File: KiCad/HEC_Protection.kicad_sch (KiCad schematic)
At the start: 16 parts, among them U11 74LS00, U11 74LS32, U12 74LS04, U17 74LS74, U18 74LS74, U19 74LS30, U22 74LS02, U23 74LS30, U24 74LS74, U25 74LS541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

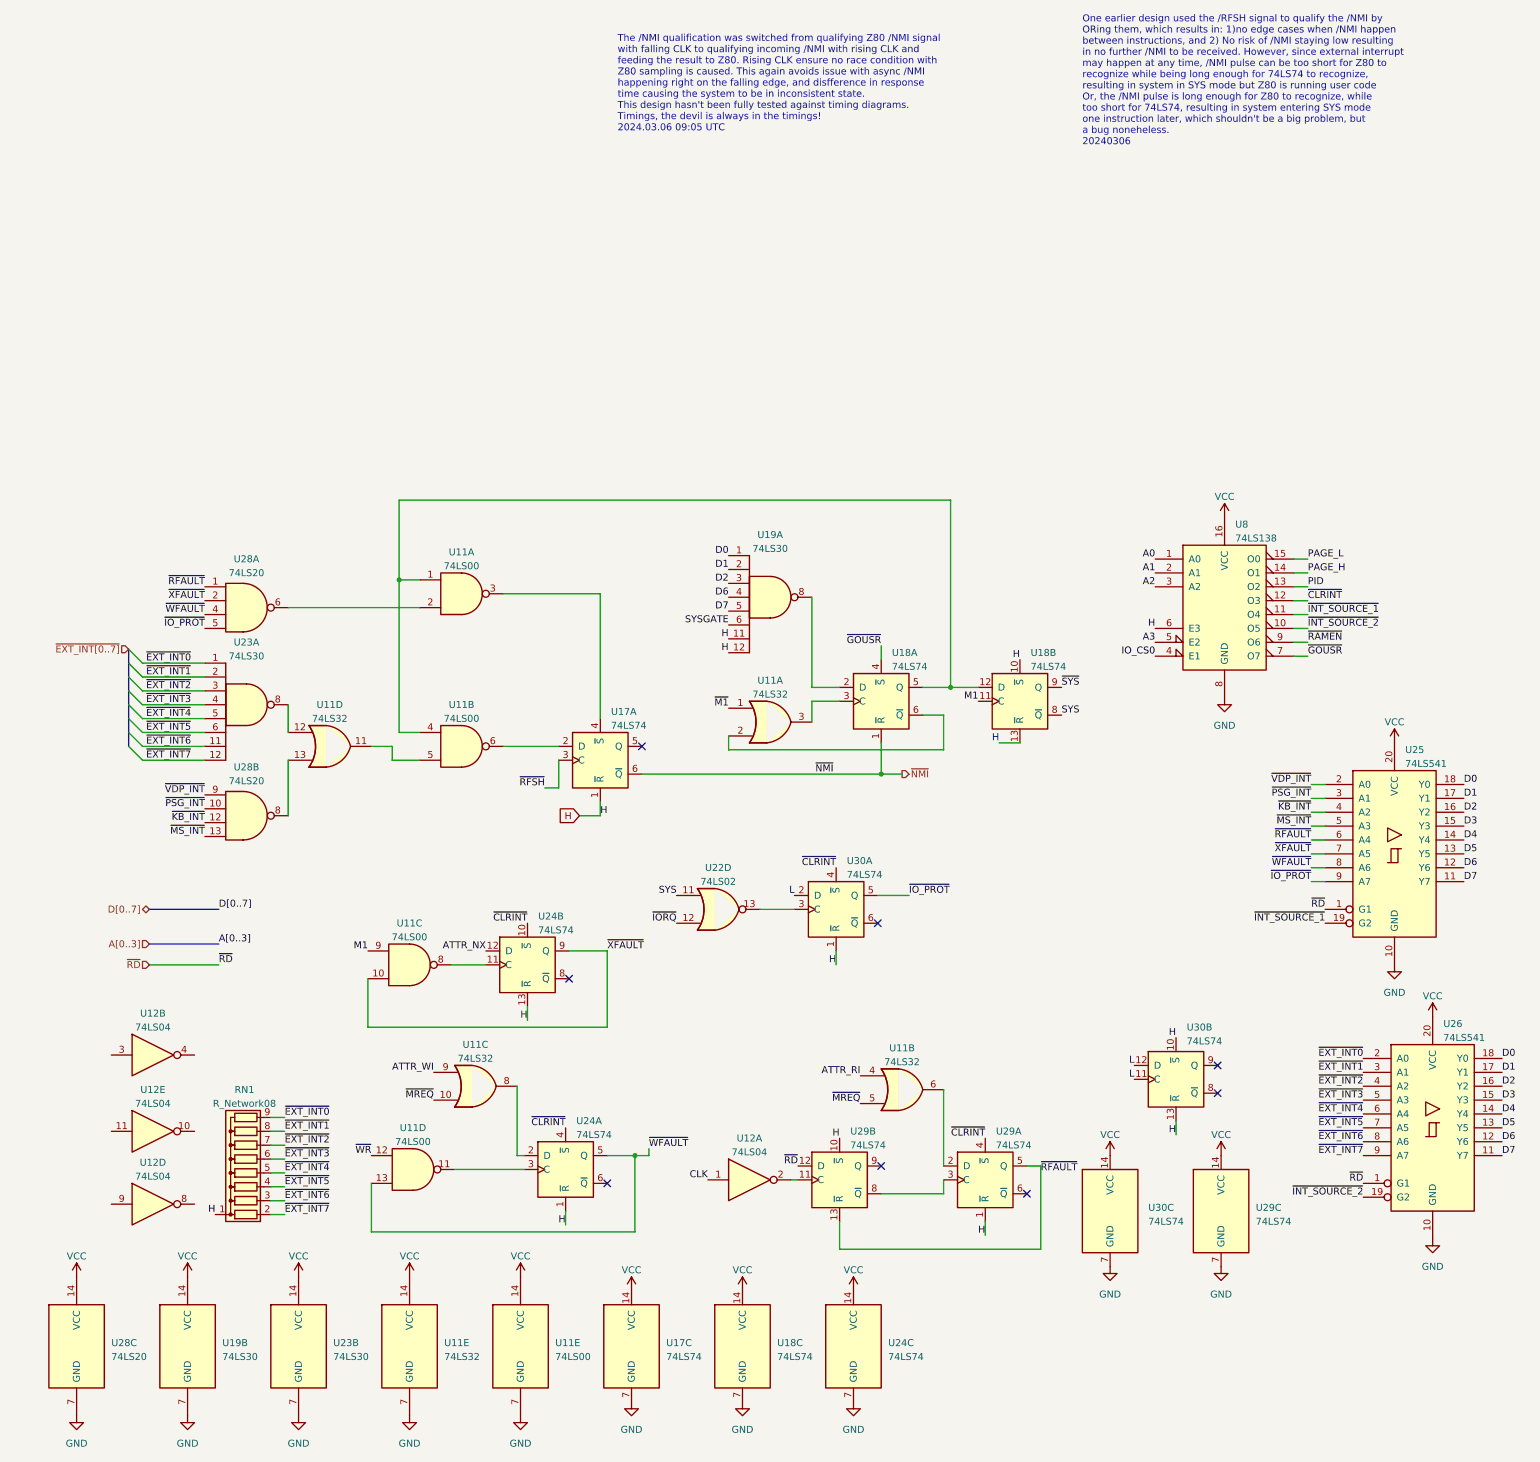
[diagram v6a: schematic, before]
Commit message: IO implementation
Implemented most of IO functions, add connections between the schematics.
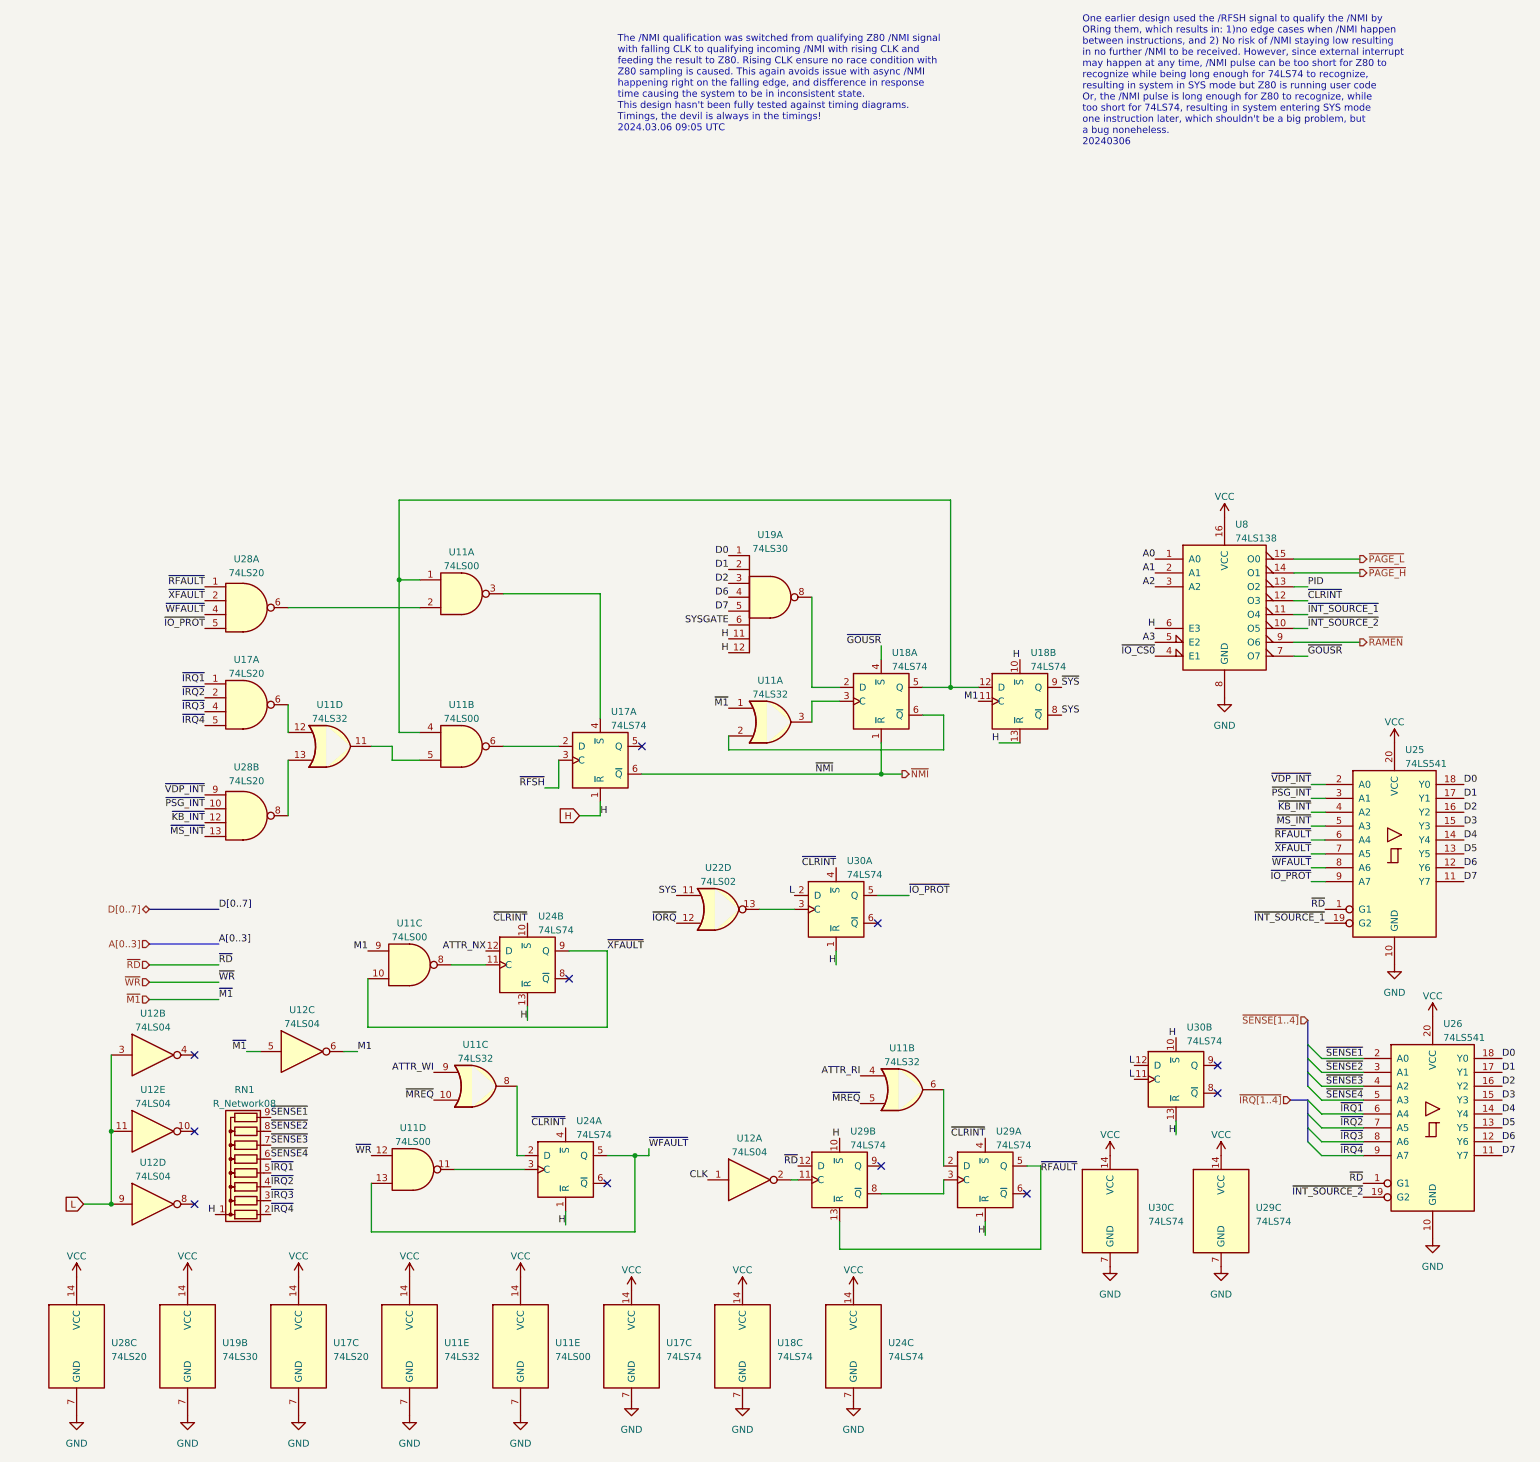
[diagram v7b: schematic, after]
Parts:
- removed U23: 74LS30, Package_DIP:DIP-14_W7.62mm_Socket, symbol 74xx:74LS30
- added unit 3 of U12
- added U17: 74LS20, symbol 74xx:74LS20
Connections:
- net GND: now also U17.7 (GND)
- net L: now also U12.11, U12.3, U12.9
- net M1: now also U12.6
- net VCC: now also U17.14 (VCC)
- net ~{M1}: now also U12.5
- net at U11.12: now also U17.6
- net IO_CS0 renamed ~{IO_CS0}
- net PAGE_H renamed ~{PAGE_H}
- net PAGE_L renamed ~{PAGE_L}
- net ~{EXT_INT0} renamed ~{SENSE1}
- net ~{EXT_INT1} renamed ~{SENSE2}
- net ~{EXT_INT2} renamed ~{SENSE3}
- net ~{EXT_INT3} renamed ~{SENSE4}
- net ~{EXT_INT4} renamed ~{IRQ1}
- net ~{IRQ1}: now also U17.1
- net ~{EXT_INT5} renamed ~{IRQ2}
- net ~{IRQ2}: now also U17.2
- net ~{EXT_INT6} renamed ~{IRQ3}
- net ~{IRQ3}: now also U17.4
- net ~{EXT_INT7} renamed ~{IRQ4}
- net ~{IRQ4}: now also U17.5
- no-connect marks 8 -> 11

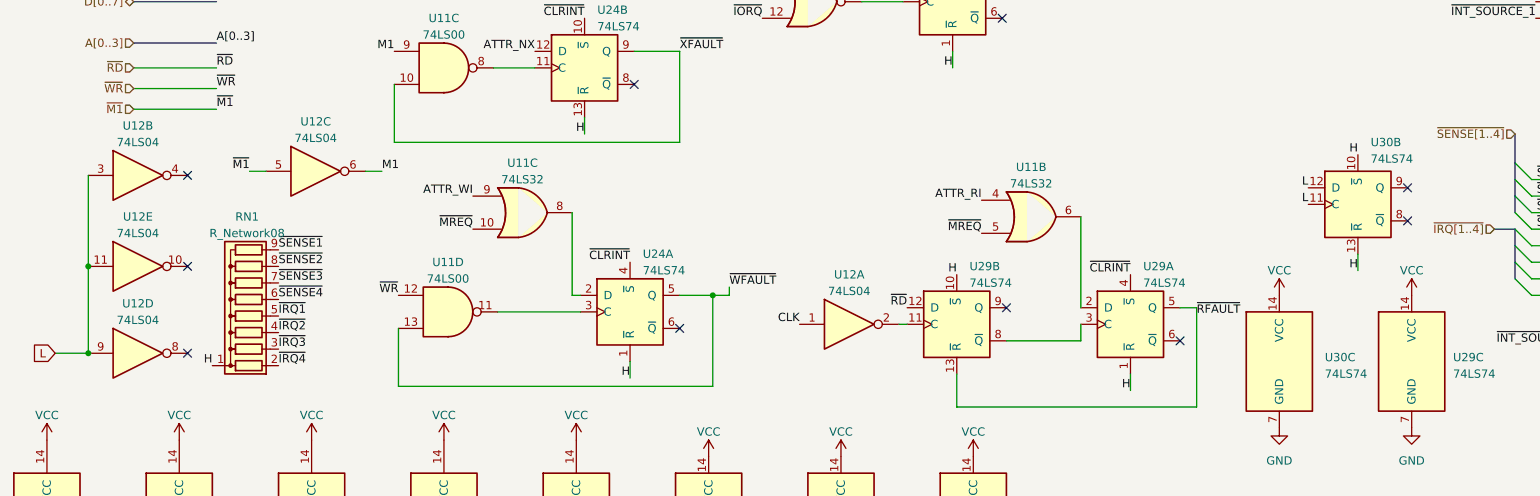
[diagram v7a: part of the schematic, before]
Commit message: Add wait state generator
Add circuit to generate 0 to 15 wait states or use external wait input.
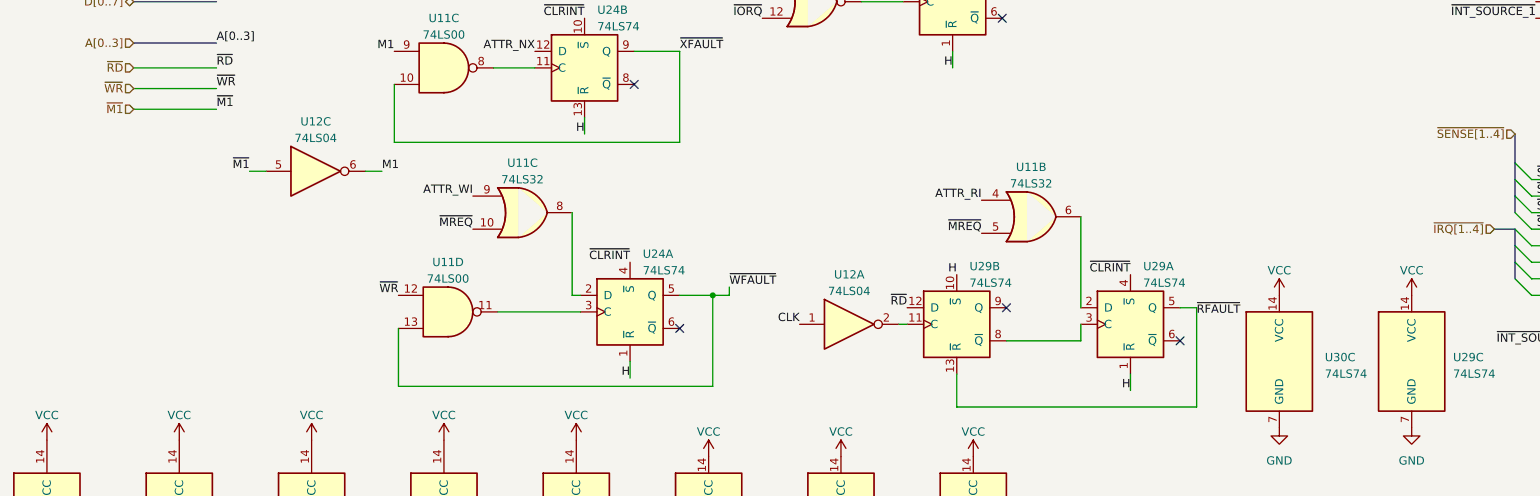
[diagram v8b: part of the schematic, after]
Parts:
- removed RN1: R_Network08, Resistor_THT:R_Array_SIP9, symbol Device:R_Network08
- removed unit 5 of U12
- removed unit 2 of U12
- removed unit 4 of U12
- removed unit 2 of U30
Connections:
- no-connect marks 11 -> 6
